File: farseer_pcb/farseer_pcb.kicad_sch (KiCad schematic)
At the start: 0 parts

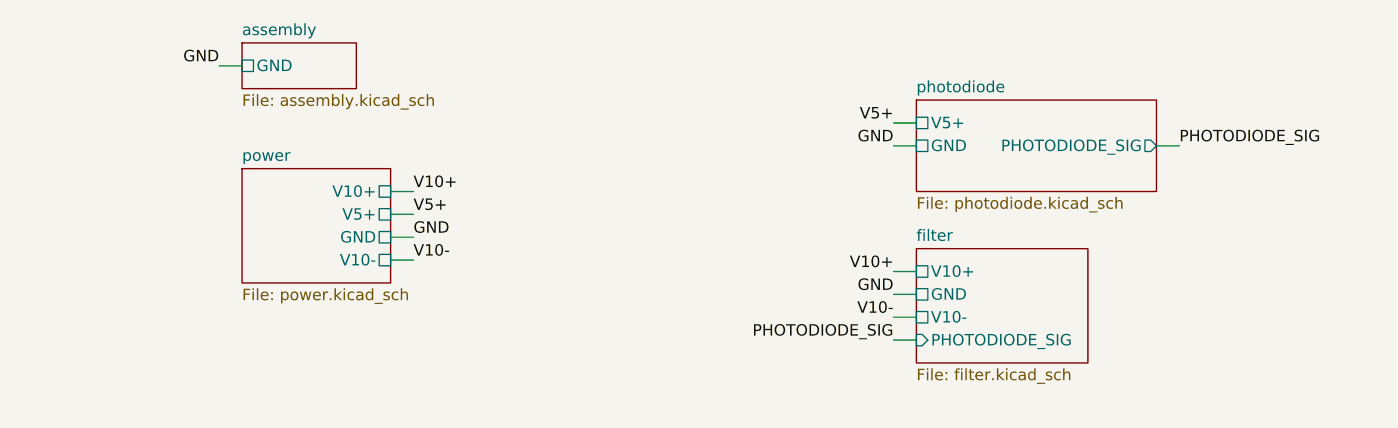
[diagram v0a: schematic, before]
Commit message: Begin board resize
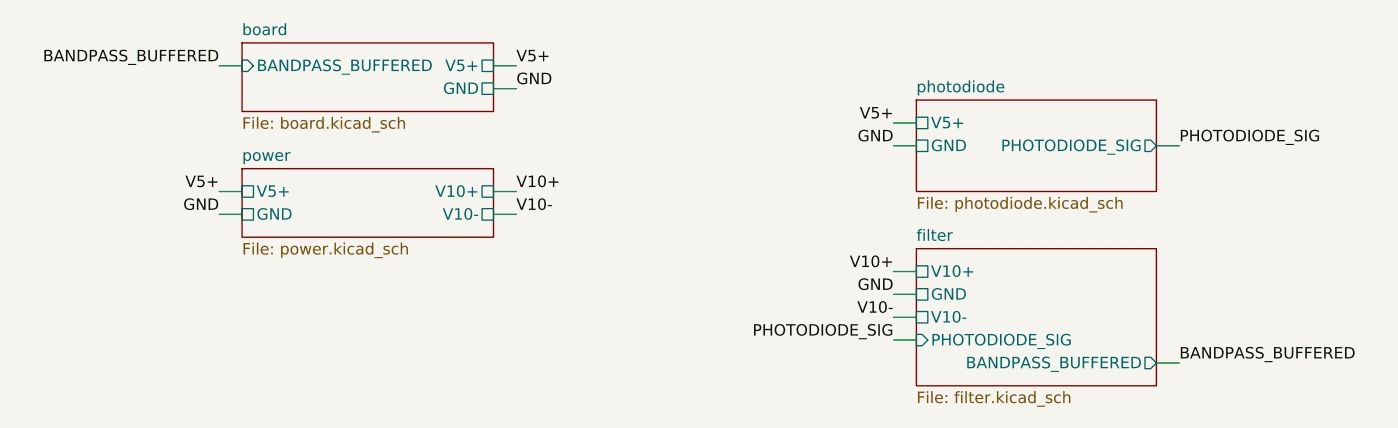
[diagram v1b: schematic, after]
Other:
- sheet assembly renamed board
- sheet board: file assembly.kicad_sch -> board.kicad_sch
- sheet board ports: added BANDPASS_BUFFERED, V5+; removed none
- sheet filter ports: added BANDPASS_BUFFERED; removed none
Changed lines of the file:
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@@
 	(title_block
 		(title "farseer_pcb")
-		(date "2025-05-16")
+		(date "2025-05-20")
 		(rev "1.0")
 		(company "Mechatronic Magic")
@@
 	(wire
 		(pts
-			(xy 113.03 111.76) (xy 110.49 111.76)
+			(xy 93.98 90.17) (xy 91.44 90.17)
+		)
+		(stroke
+			(width 0)
+			(type default)
+		)
+	)
+	(wire
+		(pts
+			(xy 121.92 90.17) (xy 124.46 90.17)
+		)
+		(stroke
+			(width 0)
+			(type default)
+		)
+	)
+	(wire
+		(pts
+			(xy 124.46 106.68) (xy 121.92 106.68)
 		)
 		(stroke
@@
 	(wire
 		(pts
-			(xy 113.03 109.22) (xy 110.49 109.22)
+			(xy 195.58 123.19) (xy 198.12 123.19)
+		)
+		(stroke
+			(width 0)
+			(type default)
+		)
+	)
+	(wire
+		(pts
+			(xy 91.44 106.68) (xy 93.98 106.68)
 		)
 		(stroke
@@
 	(wire
 		(pts
-			(xy 91.44 90.17) (xy 93.98 90.17)
+			(xy 121.92 92.71) (xy 124.46 92.71)
 		)
 		(stroke
@@
 	(wire
 		(pts
-			(xy 113.03 104.14) (xy 110.49 104.14)
+			(xy 124.46 104.14) (xy 121.92 104.14)
 		)
 		(stroke
@@
 	(wire
 		(pts
-			(xy 110.49 106.68) (xy 113.03 106.68)
+			(xy 93.98 104.14) (xy 91.44 104.14)
 		)
 		(stroke
@@
 	)
 	(label "V10-"
-		(at 113.03 111.76 0)
+		(at 124.46 106.68 0)
 		(effects
 			(font
@@
 	)
 	(label "GND"
-		(at 113.03 109.22 0)
-		(effects
-			(font
-				(size 1.27 1.27)
-			)
-			(justify left bottom)
+		(at 91.44 106.68 180)
+		(effects
+			(font
+				(size 1.27 1.27)
+			)
+			(justify right bottom)
 		)
 	)
@@
 	)
 	(label "GND"
-		(at 91.44 90.17 180)
-		(effects
-			(font
-				(size 1.27 1.27)
-			)
-			(justify right bottom)
+		(at 124.46 92.71 0)
+		(effects
+			(font
+				(size 1.27 1.27)
+			)
+			(justify left bottom)
 		)
 	)
@@
 	)
 	(label "V10+"
-		(at 113.03 104.14 0)
-		(effects
-			(font
-				(size 1.27 1.27)
-			)
-			(justify left bottom)
+		(at 124.46 104.14 0)
+		(effects
+			(font
+				(size 1.27 1.27)
+			)
+			(justify left bottom)
+		)
+	)
+	(label "BANDPASS_BUFFERED"
+		(at 91.44 90.17 180)
+		(effects
+			(font
+				(size 1.27 1.27)
+			)
+			(justify right bottom)
 		)
 	)
@@
 	)
 	(label "V5+"
-		(at 113.03 106.68 0)
-		(effects
-			(font
-				(size 1.27 1.27)
-			)
-			(justify left bottom)
+		(at 91.44 104.14 180)
+		(effects
+			(font
+				(size 1.27 1.27)
+			)
+			(justify right bottom)
 		)
 	)
@@
 		)
 	)
+	(label "BANDPASS_BUFFERED"
+		(at 198.12 123.19 0)
+		(effects
+			(font
+				(size 1.27 1.27)
+			)
+			(justify left bottom)
+		)
+	)
+	(label "V5+"
+		(at 124.46 90.17 0)
+		(effects
+			(font
+				(size 1.27 1.27)
+			)
+			(justify left bottom)
+		)
+	)
 	(sheet
 		(at 93.98 87.63)
-		(size 12.7 5.08)
+		(size 27.94 7.62)
 		(exclude_from_sim no)
 		(in_bom yes)
@@
 			(color 0 0 0 0.0000)
 		)
-		(property "Sheetname" "assembly"
+		(property "Sheetname" "board"
 			(at 93.98 86.9184 0)
 			(effects
@@
 			)
 		)
-		(property "Sheetfile" "assembly.kicad_sch"
-			(at 93.98 93.2946 0)
+		(property "Sheetfile" "board.kicad_sch"
+			(at 93.98 95.8346 0)
 			(effects
 				(font
@@
 		)
 		(pin "GND" passive
+			(at 121.92 92.71 0)
+			(effects
+				(font
+					(size 1.27 1.27)
+				)
+				(justify right)
+			)
+		)
+		(pin "V5+" passive
+			(at 121.92 90.17 0)
+			(effects
+				(font
+					(size 1.27 1.27)
+				)
+				(justify right)
+			)
+		)
+		(pin "BANDPASS_BUFFERED" input
 			(at 93.98 90.17 180)
 			(effects
@@
 	(sheet
 		(at 168.91 110.49)
-		(size 19.05 12.7)
+		(size 26.67 15.24)
 		(exclude_from_sim no)
 		(in_bom yes)
@@
 		)
 		(property "Sheetfile" "filter.kicad_sch"
-			(at 168.91 123.7746 0)
+			(at 168.91 126.3146 0)
 			(effects
 				(font
@@
 				)
 				(justify left)
+			)
+		)
+		(pin "BANDPASS_BUFFERED" output
+			(at 195.58 123.19 0)
+			(effects
+				(font
+					(size 1.27 1.27)
+				)
+				(justify right)
 			)
 		)
@@
 	(sheet
 		(at 93.98 101.6)
-		(size 16.51 12.7)
+		(size 27.94 7.62)
 		(exclude_from_sim no)
 		(in_bom yes)
@@
 		)
 		(property "Sheetfile" "power.kicad_sch"
-			(at 93.98 114.8846 0)
+			(at 93.98 109.8046 0)
 			(effects
 				(font
@@
 		)
 		(pin "GND" passive
-			(at 110.49 109.22 0)
+			(at 93.98 106.68 180)
+			(effects
+				(font
+					(size 1.27 1.27)
+				)
+				(justify left)
+			)
+		)
+		(pin "V5+" passive
+			(at 93.98 104.14 180)
+			(effects
+				(font
+					(size 1.27 1.27)
+				)
+				(justify left)
+			)
+		)
+		(pin "V10+" passive
+			(at 121.92 104.14 0)
 			(effects
 				(font
@@
 			)
 		)
-		(pin "V5+" passive
-			(at 110.49 106.68 0)
-			(effects
-				(font
-					(size 1.27 1.27)
-				)
-				(justify right)
-			)
-		)
-		(pin "V10+" passive
-			(at 110.49 104.14 0)
-			(effects
-				(font
-					(size 1.27 1.27)
-				)
-				(justify right)
-			)
-		)
 		(pin "V10-" passive
-			(at 110.49 111.76 0)
-			(effects
-				(font
+			(at 121.92 106.68 0)
+			(effects
+				(font
